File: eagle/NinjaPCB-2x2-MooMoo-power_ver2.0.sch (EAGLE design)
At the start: 32 parts, among them J3 HEATER, Q1 S8550, Q2 IRF520NPBF, Q4 S8550, Q5 IRF520NPBF, Q6 S8550, Q7 S8550, Q8 S8550, U1 CJT1117-3.3-SOT223

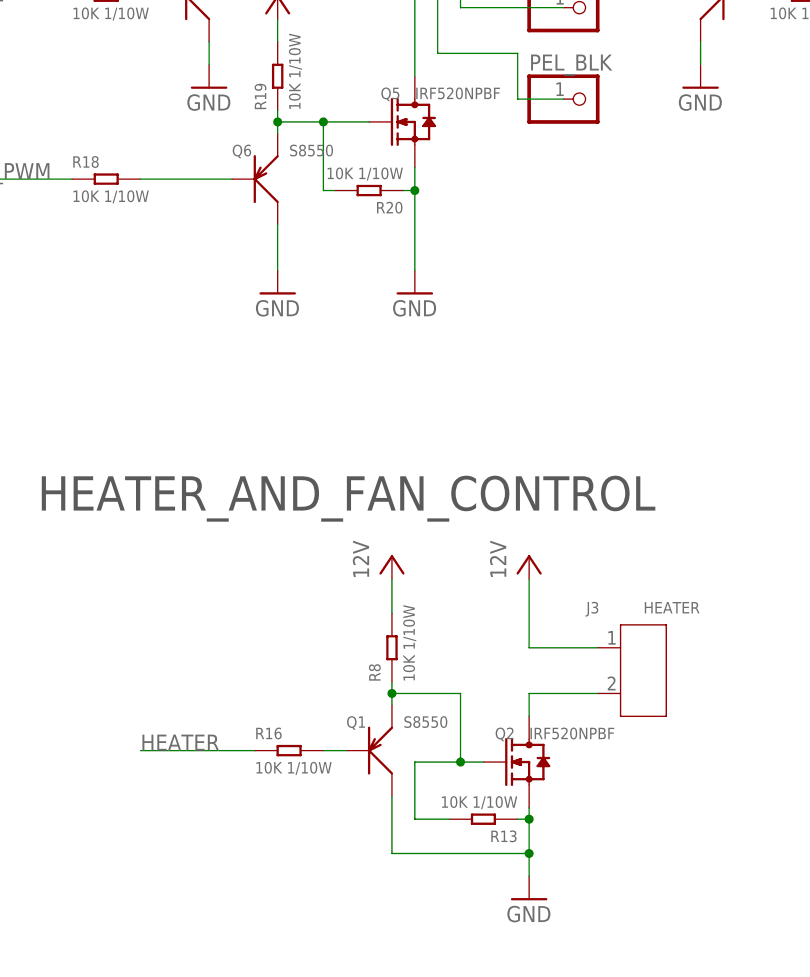
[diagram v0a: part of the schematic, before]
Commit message: change values of MOSFET G-S reg
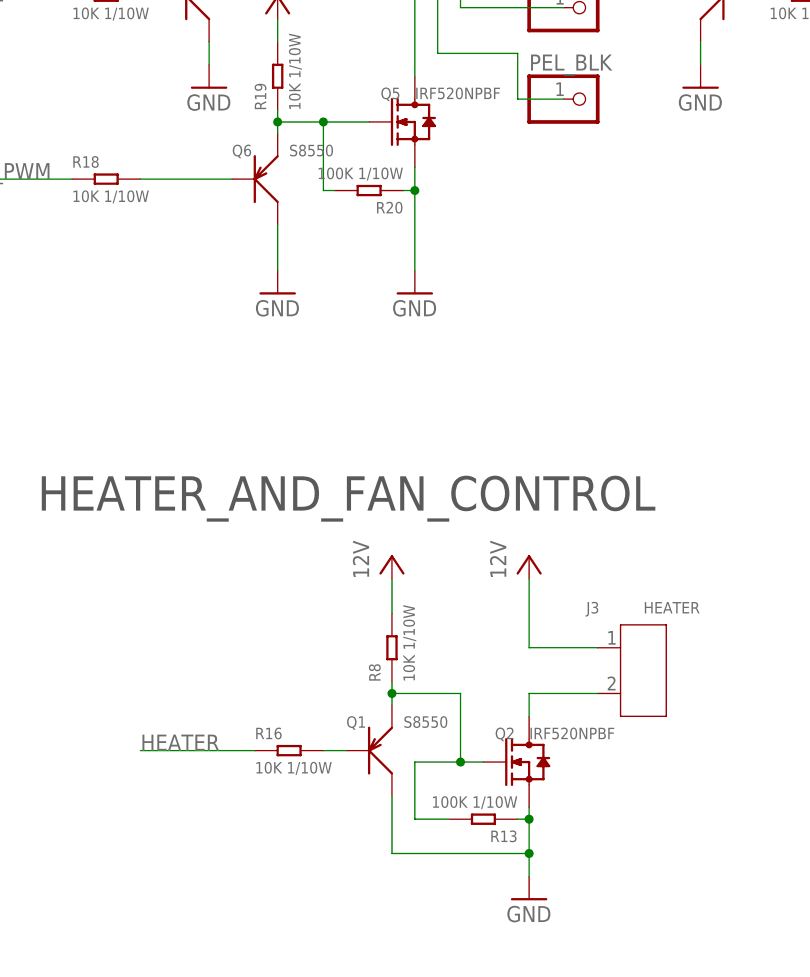
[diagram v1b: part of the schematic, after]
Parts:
- R13, R20: value 10K 1/10W -> 100K 1/10W; device Seeed-Resistor:SMD-RES-10K-5%-1/10W(0603) -> Seeed-Resistor:SMD-RES-100K-5%-1/10W(0603)
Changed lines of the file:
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@@
 <setting verticaltext="up"/>
 </settings>
-<grid distance="0.05" unitdist="inch" unit="inch" style="lines" multiple="1" display="no" altdistance="0.01" altunitdist="inch" altunit="inch"/>
+<grid distance="0.1" unitdist="inch" unit="inch" style="lines" multiple="1" display="no" altdistance="0.01" altunitdist="inch" altunit="inch"/>
 <layers>
 <layer number="1" name="Top" color="4" fill="1" visible="no" active="no"/>
@@
 <part name="Q4" library="Seeed-Transistor" deviceset="SMD-TRANSISTORS-PNP-25V-500MA-S8550(SOT-23)" device="" value="S8550"/>
 <part name="R8" library="Seeed-Resistor" deviceset="SMD-RES-10K-5%-1/10W(0603)" device="" value="10K 1/10W"/>
-<part name="R13" library="Seeed-Resistor" deviceset="SMD-RES-10K-5%-1/10W(0603)" device="" value="10K 1/10W"/>
+<part name="R13" library="Seeed-Resistor" deviceset="SMD-RES-100K-5%-1/10W(0603)" device="" value="100K 1/10W"/>
 <part name="Q5" library="Seeed-Transistor" deviceset="DIP-MOSFET-N-CH-100V-9.7A-IRF520NPBF(TO-220AB)" device="CORRECT" value="IRF520NPBF"/>
 <part name="GND3" library="supply1" deviceset="GND" device=""/>
@@
 <part name="Q6" library="Seeed-Transistor" deviceset="SMD-TRANSISTORS-PNP-25V-500MA-S8550(SOT-23)" device="" value="S8550"/>
 <part name="R19" library="Seeed-Resistor" deviceset="SMD-RES-10K-5%-1/10W(0603)" device="" value="10K 1/10W"/>
-<part name="R20" library="Seeed-Resistor" deviceset="SMD-RES-10K-5%-1/10W(0603)" device="" value="10K 1/10W"/>
+<part name="R20" library="Seeed-Resistor" deviceset="SMD-RES-100K-5%-1/10W(0603)" device="" value="100K 1/10W"/>
 <part name="RELAY" library="PCR-Switch" deviceset="NEC-RELAY2" device="EP2" value="NEC-RELAY2EP2"/>
 <part name="D1" library="Seeed-Diode" deviceset="DIODE-GEN-PURPOSE-1KV-1A(DO-214AC)" device="" value="1N4007"/>
